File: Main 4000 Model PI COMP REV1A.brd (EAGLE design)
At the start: 160 x 100 mm, 120 parts, among them IC1 QUAD_OPAMPD, IC2 7818TV, IC3 TL331, IC4 TUSB2036, Q1 16MHZ, Q2 TIP120, Q3 BC846, Q4 BC846, U1 RFM69HCW, U3 MAX98306ETD+, U4 ADS1015

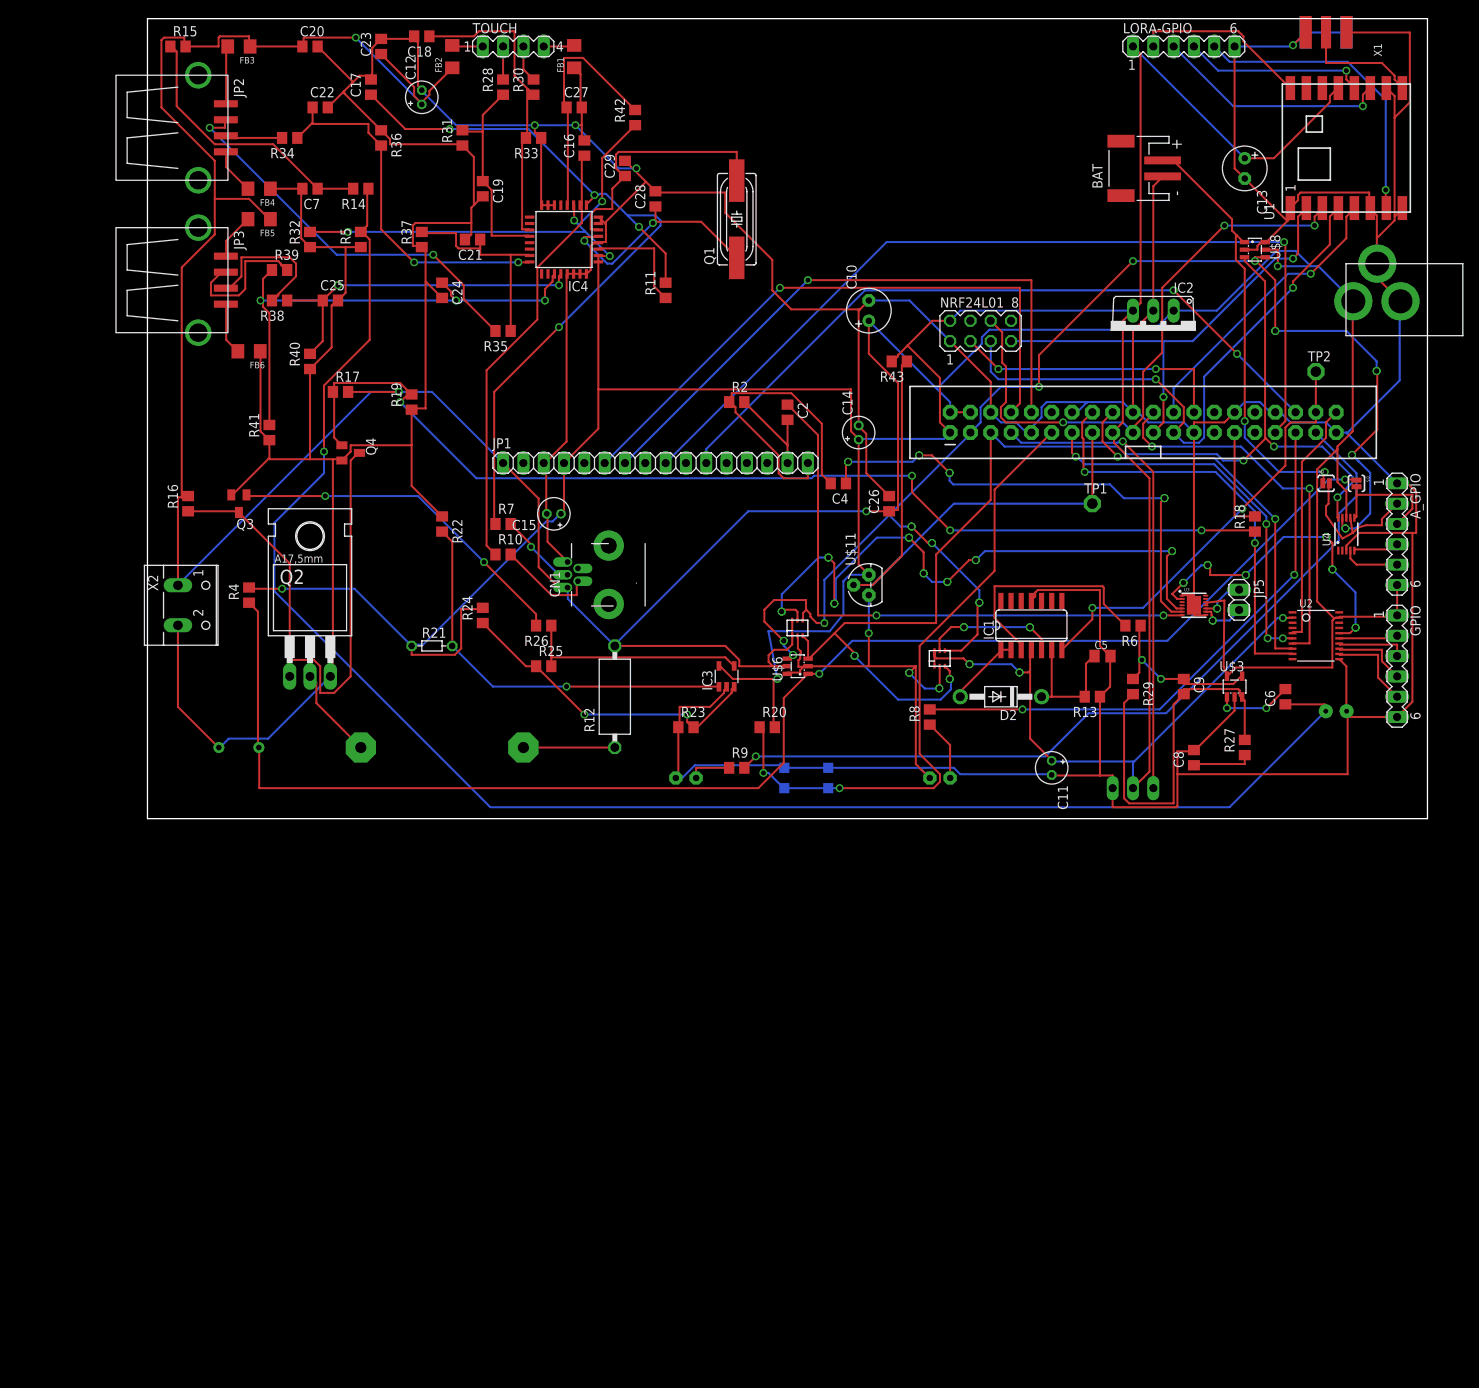
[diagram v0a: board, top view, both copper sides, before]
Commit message: Added boost circuit
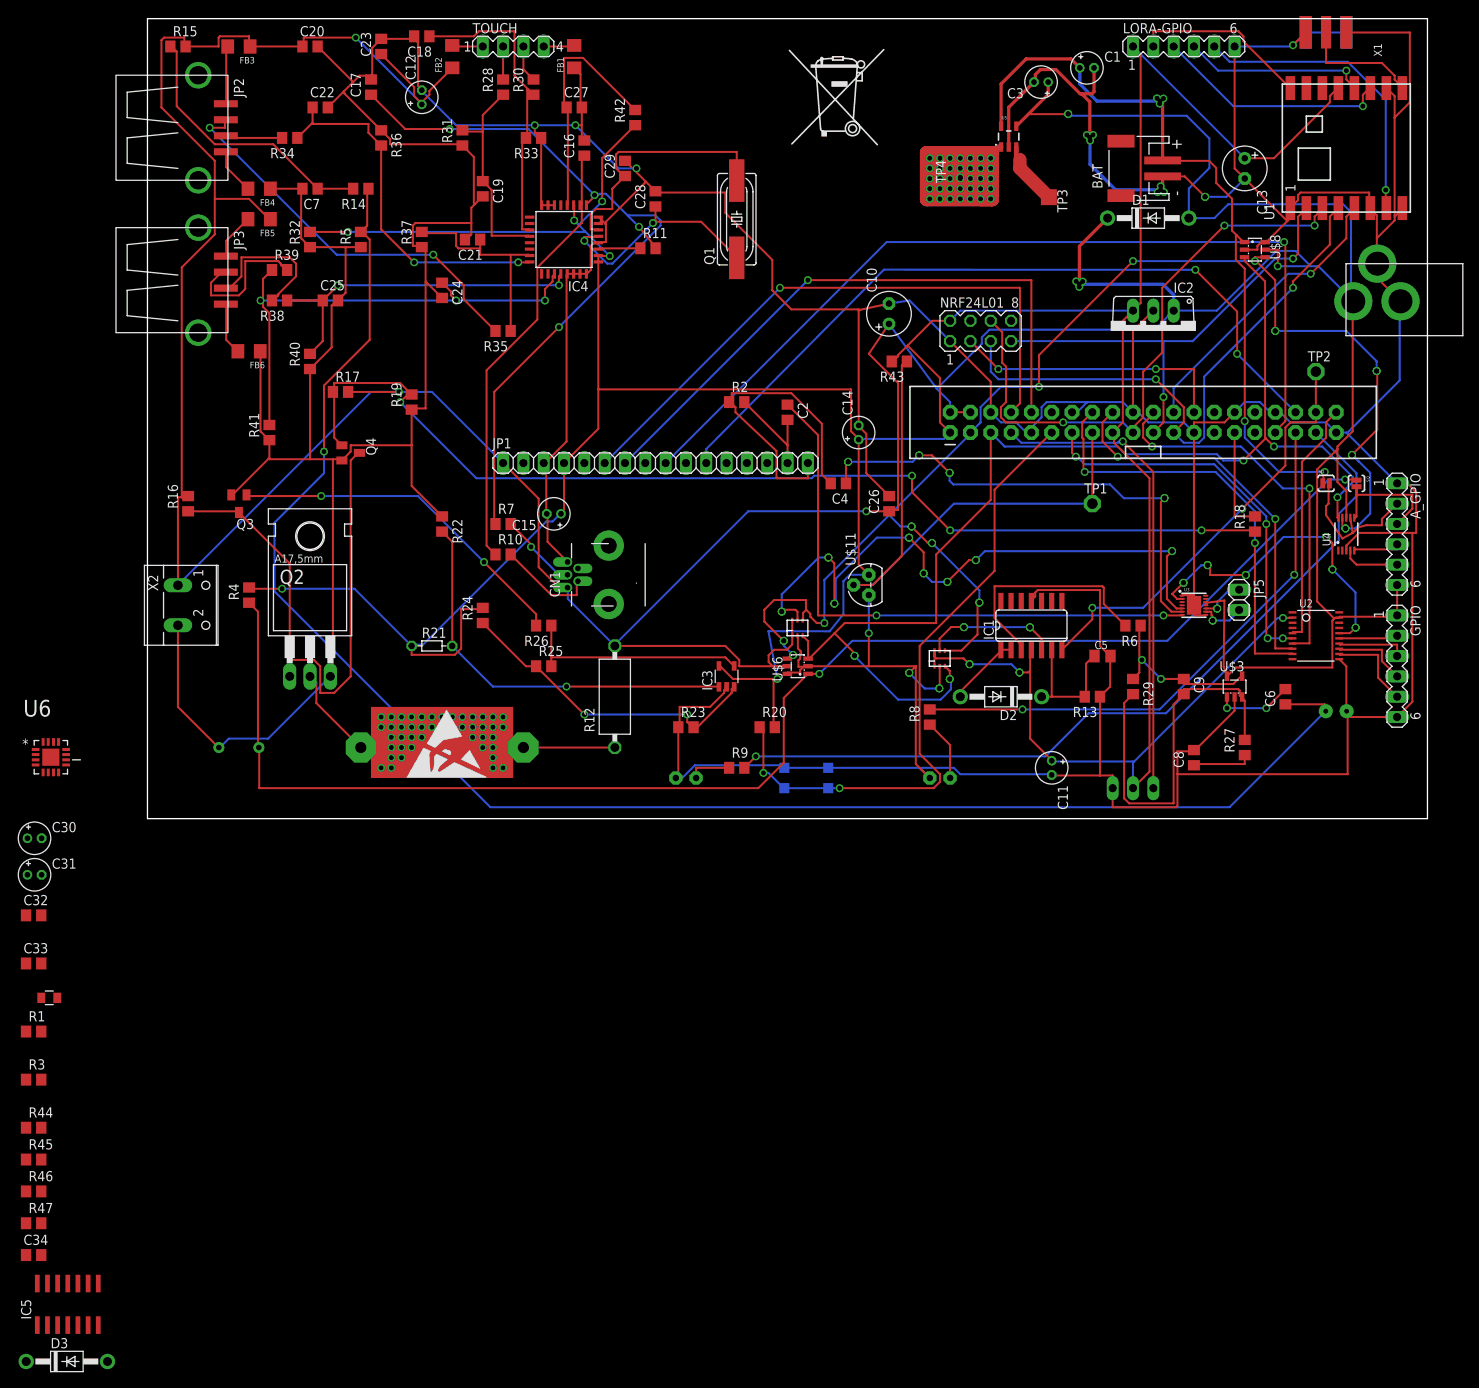
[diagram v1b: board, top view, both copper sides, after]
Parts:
- added C1, C3, C30, C31: (no value), rcl:E1,8-4
- added C32: 0.1uF, rcl:C0805
- added C33: 100uF, rcl:C0805
- added C34: (no value), rcl:C0805
- added D1, D3: 1N4004, adafruit:DO41-10
- added FB7: 6.8uH, ELL-i-Passives:SMD0805-A
- added IC5: DG200CJD, linear:SO14
- added R1, R3: 47k, rcl:R0805
- added R44, R45, R46, R47: (no value), rcl:R0805
- added TP3, TP4, TP5: TPTP20SQ, testpad:TP20SQ
- added U$13, U$14: (no value), logo:ESD_10.00
- added U$15: (no value), logo:MUELLTONNE
- added U5: MAX1555, SparkFun-PowerIC:SOT23-5
- added U6: TPS61030RSAR, Texas Instruments_By_element14_Batch_1:QFN65P400X400X100-17N
- moved R11 5.70 mm to (62.6, 71.3), turned to 0 degrees
- moved C10 2.55 mm to (92.7, 63.1)
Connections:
- new net ENABLE: IC5.9, R45.1, U6.11
- new net FB: R46.2, R47.1, U6.14
- new net N$193: D3.C, IC5.14
- new net N$196: FB7.P$2, U6.3
- new net N$197: R1.1, U6.17
- new net N$198: R3.1, R44.2, U6.9
- new net N$95: TP3.TP, U5.3
- new net N$96: TP4.TP, TP5.TP, U5.1
- new net VCC: C3.+, D1.A, D3.A, U$2.TIP, U5.4
- net 5V: now also C30.+, C31.+, C34.1, D1.C, R47.2, U6.1, U6.15, U6.16; no longer U$2.TIP
- net GND: now also C1.-, C3.-, C30.-, C31.-, C32.2, C33.2, C34.2, IC5.10, IC5.3, IC5.7, R44.1, R46.1, U5.2, U6.10, U6.13, U6.5, U6.6, U6.7
- net VBAT: now also C1.+, C32.1, C33.1, FB7.P$1, IC5.12, R1.2, R3.2, R45.2, U5.5, U6.8
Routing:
- net N$96: track 0.00 -> 134.7 mm, vias 0 -> 1
- net VCC: track 0.00 -> 76.8 mm, vias 0 -> 1
- net VBAT: track 54.5 -> 94.4 mm, vias 2 -> 3
- net GND: track 1001.3 -> 1039.5 mm, vias 7 -> 10
- net 5V: track 511.9 -> 534.3 mm, vias 4 -> 6
- net N$105: track 13.8 -> 5.50 mm
- net N$95: track 0.00 -> 7.96 mm
- net PWRSTAT: track 89.9 -> 95.2 mm
- net N$103: track 101.5 -> 96.5 mm
- net AUDIO_GND: track 39.6 -> 40.2 mm

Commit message: Laid out booster circuit
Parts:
- moved R47 183.2 mm to (95.6, 96.0), turned to 90 degrees
- moved C34 181.2 mm to (90.2, 93.5), turned to 270 degrees
- moved R44 177.7 mm to (103.6, 94.4)
- moved D3 175.6 mm to (79.2, 83.3), turned to 90 degrees
- moved R46 175.4 mm to (94.7, 90.9)
- moved R3 173.4 mm to (100.8, 97.2), turned to 180 degrees
- moved IC5 167.4 mm to (85.4, 76.9), turned to 90 degrees
- moved R45 161.2 mm to (85.2, 84.3), turned to 90 degrees
- moved FB7 156.3 mm to (101.0, 85.2)
- moved R1 152.4 mm to (88.3, 86.2), turned to 270 degrees
- moved U6 139.2 mm to (100.5, 89.5), turned to 90 degrees
- moved C31 138.3 mm to (93.6, 79.7)
- moved C33 136.7 mm to (90.2, 70.1)
- moved C30 132.6 mm to (93.6, 74.9)
- moved C32 126.2 mm to (81.5, 70.2), turned to 180 degrees
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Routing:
- net VBAT: track 94.4 -> 180.2 mm, vias 3 -> 7
- net GND: track 1039.5 -> 1121.9 mm, vias 10 -> 18
- net VCC: track 76.8 -> 152.6 mm, vias 1 -> 2
- net 5V: track 534.3 -> 595.6 mm, vias 6 -> 9
- net ENABLE: track 0.00 -> 41.5 mm
- net N$197: track 0.00 -> 13.2 mm, vias 0 -> 2
- net N$193: track 0.00 -> 12.4 mm
- net N$198: track 0.00 -> 9.86 mm
- net FB: track 0.00 -> 8.29 mm
- net N$196: track 0.00 -> 2.78 mm
- net PWRSTAT: track 95.2 -> 97.0 mm
